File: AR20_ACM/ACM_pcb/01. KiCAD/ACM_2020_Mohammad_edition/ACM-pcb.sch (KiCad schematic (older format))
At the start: 32 parts, among them J1 TC2030-MCP-NL, P1 Conn_02x15_Odd_Even, Q1 Q_PMOS_DGS, U1 ATmega328P-AU, U2 MCP25625-x-SS, U3 NCV890430MW50TXG, Y1 16.0Mhz

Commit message: ACM-pcb full connected
ACM -12.01
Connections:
- net labels added: U-Pin29
- wire segments 103 -> 102
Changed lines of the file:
@@
 	5275 4150 5275 4225
-$Comp
-L ACM_Y2020V0.1-rescue:+12V-power #PWR015
-U 1 1 5D3DBA57
-P 6100 1175
-F 0 "#PWR015" H 6100 1025 50  0001 C CNN
-F 1 "+12V" V 6100 1375 50  0000 C CNN
-F 2 "" H 6100 1175 50  0001 C CNN
-F 3 "" H 6100 1175 50  0001 C CNN
-	1    6100 1175
-	0    -1   -1   0
-$EndComp
-$Comp
-L ACM_Y2020V0.1-rescue:+5V-power #PWR011
-U 1 1 5D3DED37
-P 5925 1475
-F 0 "#PWR011" H 5925 1325 50  0001 C CNN
-F 1 "+5V" V 5925 1650 50  0000 C CNN
-F 2 "" H 5925 1475 50  0001 C CNN
-F 3 "" H 5925 1475 50  0001 C CNN
-	1    5925 1475
-	0    -1   -1   0
-$EndComp
 $Comp
 L ACM_Y2020V0.1-rescue:GND-power #PWR016
@@
 Text HLabel 6100 1375 0    50   Input ~ 0
 U-Pin5
-Text HLabel 6100 2375 0    50   Input ~ 0
+Text HLabel 5500 2450 0    50   Input ~ 0
 U-Pin25
-Text HLabel 5675 1050 0    50   Input ~ 0
+Text HLabel 4800 1250 0    50   Input ~ 0
 U-Pin1
 Text HLabel 6100 1275 0    50   Input ~ 0
 U-Pin3
-Text HLabel 1575 6275 0    50   Input ~ 0
-U-Pin24
 Text HLabel 1400 6400 0    50   Input ~ 0
 U-Pin30
@@
 U-Pin2
 Text HLabel 2775 5475 2    50   Input ~ 0
-U-Pin7
+U-Pin1
 Text HLabel 10775 3900 2    50   Input ~ 0
 U-Pin27
 Text HLabel 10775 4200 2    50   Input ~ 0
-U-Pin1
+U-Pin29
 Wire Wire Line
 	2775 5175 3500 5175
@@
 Wire Wire Line
 	3275 6075 3450 6075
-Text HLabel 5175 2175 0    50   Input ~ 0
+Text HLabel 6100 2375 0    50   Input ~ 0
 GREEN_LED
 Text HLabel 6100 2275 0    50   Input ~ 0
@@
 Text HLabel 6600 2375 2    50   Input ~ 0
 U-Pin26
-Text HLabel 6600 2475 2    50   Input ~ 0
+Text HLabel 7000 2475 2    50   Input ~ 0
 U-Pin28
 Text HLabel 6600 1475 2    50   Input ~ 0
 U-Pin8
-Text HLabel 6100 2575 0    50   Input ~ 0
+Text HLabel 4975 2350 0    50   Input ~ 0
 Reset
 Wire Wire Line
@@
 Text HLabel 6600 1375 2    50   Input ~ 0
 U-Pin6
-Text HLabel 6600 2275 2    50   Input ~ 0
+Text HLabel 6900 2275 2    50   Input ~ 0
 U-Pin24
 Text HLabel 6600 2175 2    50   Input ~ 0
@@
 Text HLabel 5175 2050 0    50   Input ~ 0
 CLK_MCP
-Text HLabel 5300 1925 0    50   Input ~ 0
+Text HLabel 5250 1900 0    50   Input ~ 0
 RED_LED
-Text HLabel 5325 1800 0    50   Input ~ 0
+Text HLabel 6100 1975 0    50   Input ~ 0
 BLUE_LED
 Text HLabel 6100 1875 0    50   Input ~ 0
@@
 SCK
 Connection ~ 6725 1875
-Wire Wire Line
-	6100 1475 5925 1475
-Text HLabel 6600 1575 2    50   Input ~ 0
+Text HLabel 4775 1400 2    50   Input ~ 0
 U-Pin10
 Text HLabel 1575 4775 0    50   Input ~ 0
-U-Pin5
+U-Pin7
 Text HLabel 6100 2475 0    50   Input ~ 0
 U-Pin27
-Text HLabel 6100 2175 0    50   Input ~ 0
+Text HLabel 5825 2175 0    50   Input ~ 0
 U-Pin21
 Text Notes 9275 2925 0    79   ~ 16
@@
 Wire Wire Line
 	9675 2900 9675 3650
-Text HLabel 2900 5375 2    50   Input ~ 0
-U-Pin7
-Text HLabel 6600 2575 2    50   Input ~ 0
+Text HLabel 2775 5575 2    50   Input ~ 0
+U-Pin3
+Text HLabel 4650 1600 2    50   Input ~ 0
 U-Pin30
 Wire Wire Line
@@
 Wire Wire Line
 	925  4575 925  4650
-Text HLabel 6100 2075 0    50   Input ~ 0
+Text HLabel 5825 2075 0    50   Input ~ 0
 U-Pin19
-Text HLabel 6100 1975 0    50   Input ~ 0
+Text HLabel 5450 2625 0    50   Input ~ 0
 U-Pin17
-Text HLabel 6100 1575 0    50   Input ~ 0
+Text HLabel 5775 1600 0    50   Input ~ 0
 U-Pin9
 Wire Wire Line
 	2775 6075 3275 6075
 Connection ~ 3275 6075
+Text HLabel 1400 5125 0    50   Input ~ 0
+U-Pin24
+Text HLabel 6600 1575 2    50   Input ~ 0
+Reset
+Text HLabel 6100 2575 0    50   Input ~ 0
+U-Pin29
+Text HLabel 1575 4875 0    50   Input ~ 0
+U-Pin5
+$Comp
+L ACM_Y2020V0.1-rescue:+12V-power #PWR0106
+U 1 1 5E1D7493
+P 6600 2575
+F 0 "#PWR0106" H 6600 2425 50  0001 C CNN
+F 1 "+12V" V 6600 2775 50  0000 C CNN
+F 2 "" H 6600 2575 50  0001 C CNN
+F 3 "" H 6600 2575 50  0001 C CNN
+	1    6600 2575
+	0    1    1    0
+$EndComp
+$Comp
+L ACM_Y2020V0.1-rescue:+12V-power #PWR015
+U 1 1 5D3DBA57
+P 5050 1150
+F 0 "#PWR015" H 5050 1000 50  0001 C CNN
+F 1 "+12V" V 5050 1750 50  0000 C CNN
+F 2 "" H 5050 1150 50  0001 C CNN
+F 3 "" H 5050 1150 50  0001 C CNN
+	1    5050 1150
+	0    -1   -1   0
+$EndComp
+Text HLabel 6100 1175 0    50   Input ~ 0
+U-Pin1
+$Comp
+L ACM_Y2020V0.1-rescue:+5V-power #PWR011
+U 1 1 5D3DED37
+P 6600 2475
+F 0 "#PWR011" H 6600 2325 50  0001 C CNN
+F 1 "+5V" V 6600 2650 50  0000 C CNN
+F 2 "" H 6600 2475 50  0001 C CNN
+F 3 "" H 6600 2475 50  0001 C CNN
+	1    6600 2475
+	0    1    1    0
+$EndComp
+Text HLabel 6100 1475 0    50   Input ~ 0
+U-Pin7
+$Comp
+L ACM_Y2020V0.1-rescue:GND-power #PWR0107
+U 1 1 5E243E92
+P 6600 2275
+F 0 "#PWR0107" H 6600 2025 50  0001 C CNN
+F 1 "GND" H 6605 2102 50  0000 C CNN
+F 2 "" H 6600 2275 50  0001 C CNN
+F 3 "" H 6600 2275 50  0001 C CNN
+	1    6600 2275
+	0    -1   -1   0
+$EndComp
+$Comp
+L ACM_Y2020V0.1-rescue:GND-power #PWR?
+U 1 1 5E24CDDB
+P 6100 2175
+F 0 "#PWR?" H 6100 1925 50  0001 C CNN
+F 1 "GND" H 6105 2002 50  0000 C CNN
+F 2 "" H 6100 2175 50  0001 C CNN
+F 3 "" H 6100 2175 50  0001 C CNN
+	1    6100 2175
+	0    1    1    0
+$EndComp
 $EndSCHEMATC

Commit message: final one 12.01
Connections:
- wire segments 102 -> 110
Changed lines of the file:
@@
 Wire Wire Line
 	6600 1875 6725 1875
-Text HLabel 6600 2375 2    50   Input ~ 0
+Text HLabel 8000 2400 2    50   Input ~ 0
 U-Pin26
-Text HLabel 7000 2475 2    50   Input ~ 0
+Text HLabel 7375 2525 2    50   Input ~ 0
 U-Pin28
 Text HLabel 6600 1475 2    50   Input ~ 0
@@
 Text HLabel 6600 1375 2    50   Input ~ 0
 U-Pin6
-Text HLabel 6900 2275 2    50   Input ~ 0
+Text HLabel 7875 2250 2    50   Input ~ 0
 U-Pin24
 Text HLabel 6600 2175 2    50   Input ~ 0
@@
 Text HLabel 6100 2475 0    50   Input ~ 0
 U-Pin27
-Text HLabel 5825 2175 0    50   Input ~ 0
+Text HLabel 5325 2175 0    50   Input ~ 0
 U-Pin21
 Text Notes 9275 2925 0    79   ~ 16
@@
 Text HLabel 5450 2625 0    50   Input ~ 0
 U-Pin17
-Text HLabel 5775 1600 0    50   Input ~ 0
+Text HLabel 6100 1575 0    50   Input ~ 0
 U-Pin9
 Wire Wire Line
@@
 L ACM_Y2020V0.1-rescue:+12V-power #PWR0106
 U 1 1 5E1D7493
-P 6600 2575
-F 0 "#PWR0106" H 6600 2425 50  0001 C CNN
-F 1 "+12V" V 6600 2775 50  0000 C CNN
-F 2 "" H 6600 2575 50  0001 C CNN
-F 3 "" H 6600 2575 50  0001 C CNN
-	1    6600 2575
+P 6800 2575
+F 0 "#PWR0106" H 6800 2425 50  0001 C CNN
+F 1 "+12V" V 6800 2775 50  0000 C CNN
+F 2 "" H 6800 2575 50  0001 C CNN
+F 3 "" H 6800 2575 50  0001 C CNN
+	1    6800 2575
 	0    1    1    0
 $EndComp
@@
 Text HLabel 6100 1175 0    50   Input ~ 0
 U-Pin1
-$Comp
-L ACM_Y2020V0.1-rescue:+5V-power #PWR011
-U 1 1 5D3DED37
-P 6600 2475
-F 0 "#PWR011" H 6600 2325 50  0001 C CNN
-F 1 "+5V" V 6600 2650 50  0000 C CNN
-F 2 "" H 6600 2475 50  0001 C CNN
-F 3 "" H 6600 2475 50  0001 C CNN
-	1    6600 2475
-	0    1    1    0
-$EndComp
 Text HLabel 6100 1475 0    50   Input ~ 0
 U-Pin7
@@
 L ACM_Y2020V0.1-rescue:GND-power #PWR0107
 U 1 1 5E243E92
-P 6600 2275
-F 0 "#PWR0107" H 6600 2025 50  0001 C CNN
-F 1 "GND" H 6605 2102 50  0000 C CNN
-F 2 "" H 6600 2275 50  0001 C CNN
-F 3 "" H 6600 2275 50  0001 C CNN
-	1    6600 2275
+P 7325 2125
+F 0 "#PWR0107" H 7325 1875 50  0001 C CNN
+F 1 "GND" H 7330 1952 50  0000 C CNN
+F 2 "" H 7325 2125 50  0001 C CNN
+F 3 "" H 7325 2125 50  0001 C CNN
+	1    7325 2125
 	0    -1   -1   0
 $EndComp
 $Comp
-L ACM_Y2020V0.1-rescue:GND-power #PWR?
+L ACM_Y2020V0.1-rescue:GND-power #PWR0108
 U 1 1 5E24CDDB
-P 6100 2175
-F 0 "#PWR?" H 6100 1925 50  0001 C CNN
-F 1 "GND" H 6105 2002 50  0000 C CNN
-F 2 "" H 6100 2175 50  0001 C CNN
-F 3 "" H 6100 2175 50  0001 C CNN
-	1    6100 2175
+P 6050 2175
+F 0 "#PWR0108" H 6050 1925 50  0001 C CNN
+F 1 "GND" H 6055 2002 50  0000 C CNN
+F 2 "" H 6050 2175 50  0001 C CNN
+F 3 "" H 6050 2175 50  0001 C CNN
+	1    6050 2175
 	0    1    1    0
 $EndComp
+$Comp
+L ACM_Y2020V0.1-rescue:+5V-power #PWR011
+U 1 1 5D3DED37
+P 6700 2375
+F 0 "#PWR011" H 6700 2225 50  0001 C CNN
+F 1 "+5V" V 6700 2550 50  0000 C CNN
+F 2 "" H 6700 2375 50  0001 C CNN
+F 3 "" H 6700 2375 50  0001 C CNN
+	1    6700 2375
+	0    1    1    0
+$EndComp
+Wire Wire Line
+	6700 2375 6600 2375
+Wire Wire Line
+	6600 2275 6700 2275
+Wire Wire Line
+	6700 2275 6700 2375
+Connection ~ 6700 2375
+Wire Wire Line
+	6600 2575 6800 2575
+Wire Wire Line
+	6600 2475 6700 2475
+Wire Wire Line
+	6700 2475 6700 2375
+Wire Wire Line
+	6100 2075 6100 2175
+Wire Wire Line
+	6100 2175 6050 2175
+Connection ~ 6100 2175
 $EndSCHEMATC

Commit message: Ronded corner and added a angle
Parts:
- C1, C10, C11, C2, C4, C5, C6, C7, C8, C9: symbol ACM_Y2020V0.1-rescue:C-Device -> ACM-pcb-rescue:C-Device-ACM_Y2020V0.1-rescue
- C3: symbol ACM_Y2020V0.1-rescue:C_Small-Device -> ACM-pcb-rescue:C_Small-Device-ACM_Y2020V0.1-rescue
- D1, D2: symbol ACM_Y2020V0.1-rescue:D_Zener-Device -> ACM-pcb-rescue:D_Zener-Device-ACM_Y2020V0.1-rescue
- D3: symbol ACM_Y2020V0.1-rescue:ASMB-MTB0-0A3A2-LED -> ACM-pcb-rescue:ASMB-MTB0-0A3A2-LED-ACM_Y2020V0.1-rescue
- F1: symbol ACM_Y2020V0.1-rescue:Polyfuse_Small-Device -> ACM-pcb-rescue:Polyfuse_Small-Device-ACM_Y2020V0.1-rescue
- H1: symbol ACM_Y2020V0.1-rescue:MountingHole-Mechanical -> ACM-pcb-rescue:MountingHole-Mechanical-ACM_Y2020V0.1-rescue
- J1: symbol ACM_Y2020V0.1-rescue:TC2030-MCP-NL-TC2030-MCP-NL -> ACM-pcb-rescue:TC2030-MCP-NL-TC2030-MCP-NL-ACM_Y2020V0.1-rescue
- L1, L2: symbol ACM_Y2020V0.1-rescue:L_Small-Device -> ACM-pcb-rescue:L_Small-Device-ACM_Y2020V0.1-rescue
- P1: symbol ACM_Y2020V0.1-rescue:Conn_02x15_Odd_Even-Connector_Generic -> ACM-pcb-rescue:Conn_02x15_Odd_Even-Connector_Generic-ACM_Y2020V0.1-rescue
- Q1: symbol ACM_Y2020V0.1-rescue:Q_PMOS_GSD-Device -> ACM-pcb-rescue:Q_PMOS_GSD-Device-ACM_Y2020V0.1-rescue
- R1, R2, R3, R4, R5, R6, R7: symbol ACM_Y2020V0.1-rescue:R-Device -> ACM-pcb-rescue:R-Device-ACM_Y2020V0.1-rescue
- U1: symbol ACM_Y2020V0.1-rescue:ATmega328P-AU-MCU_Microchip_ATmega -> ACM-pcb-rescue:ATmega328P-AU-MCU_Microchip_ATmega-ACM_Y2020V0.1-rescue
- U2: symbol ACM_Y2020V0.1-rescue:MCP25625-x-SS-Interface_CAN_LIN -> ACM-pcb-rescue:MCP25625-x-SS-Interface_CAN_LIN-ACM_Y2020V0.1-rescue
- U3: symbol ACM_Y2020V0.1-rescue:NCV890430MW50TXG-NCV890430MW50TXG -> ACM-pcb-rescue:NCV890430MW50TXG-NCV890430MW50TXG-ACM_Y2020V0.1-rescue
- Y1: symbol ACM_Y2020V0.1-rescue:Resonator_Small-Device -> ACM-pcb-rescue:Resonator_Small-Device-ACM_Y2020V0.1-rescue

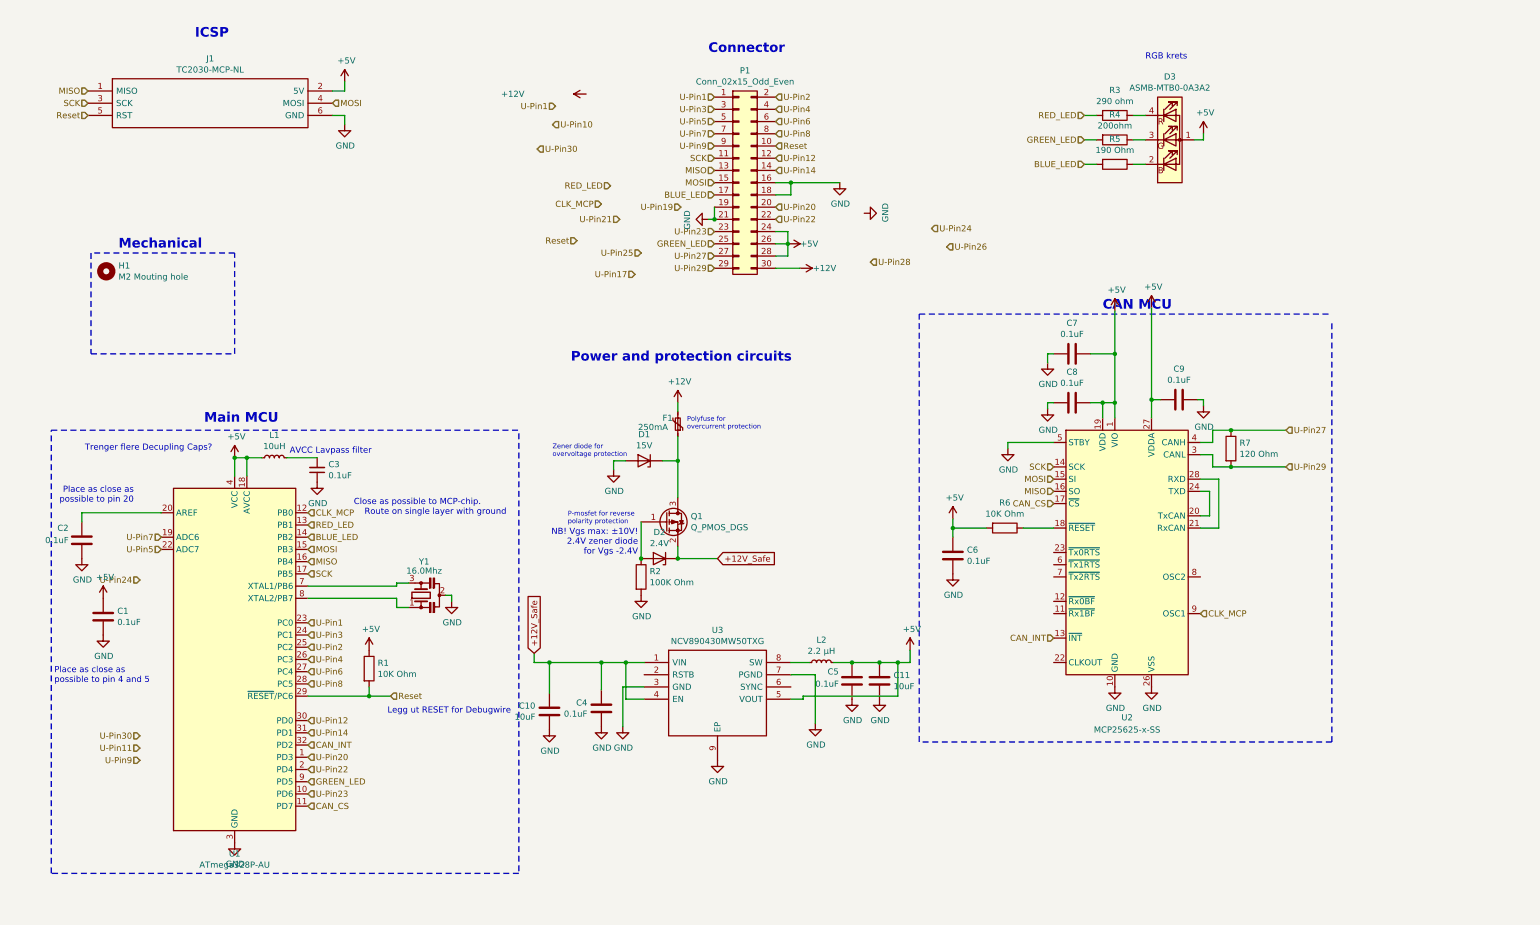
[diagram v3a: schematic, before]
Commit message: Added GND to Pin 9 and checked connector output
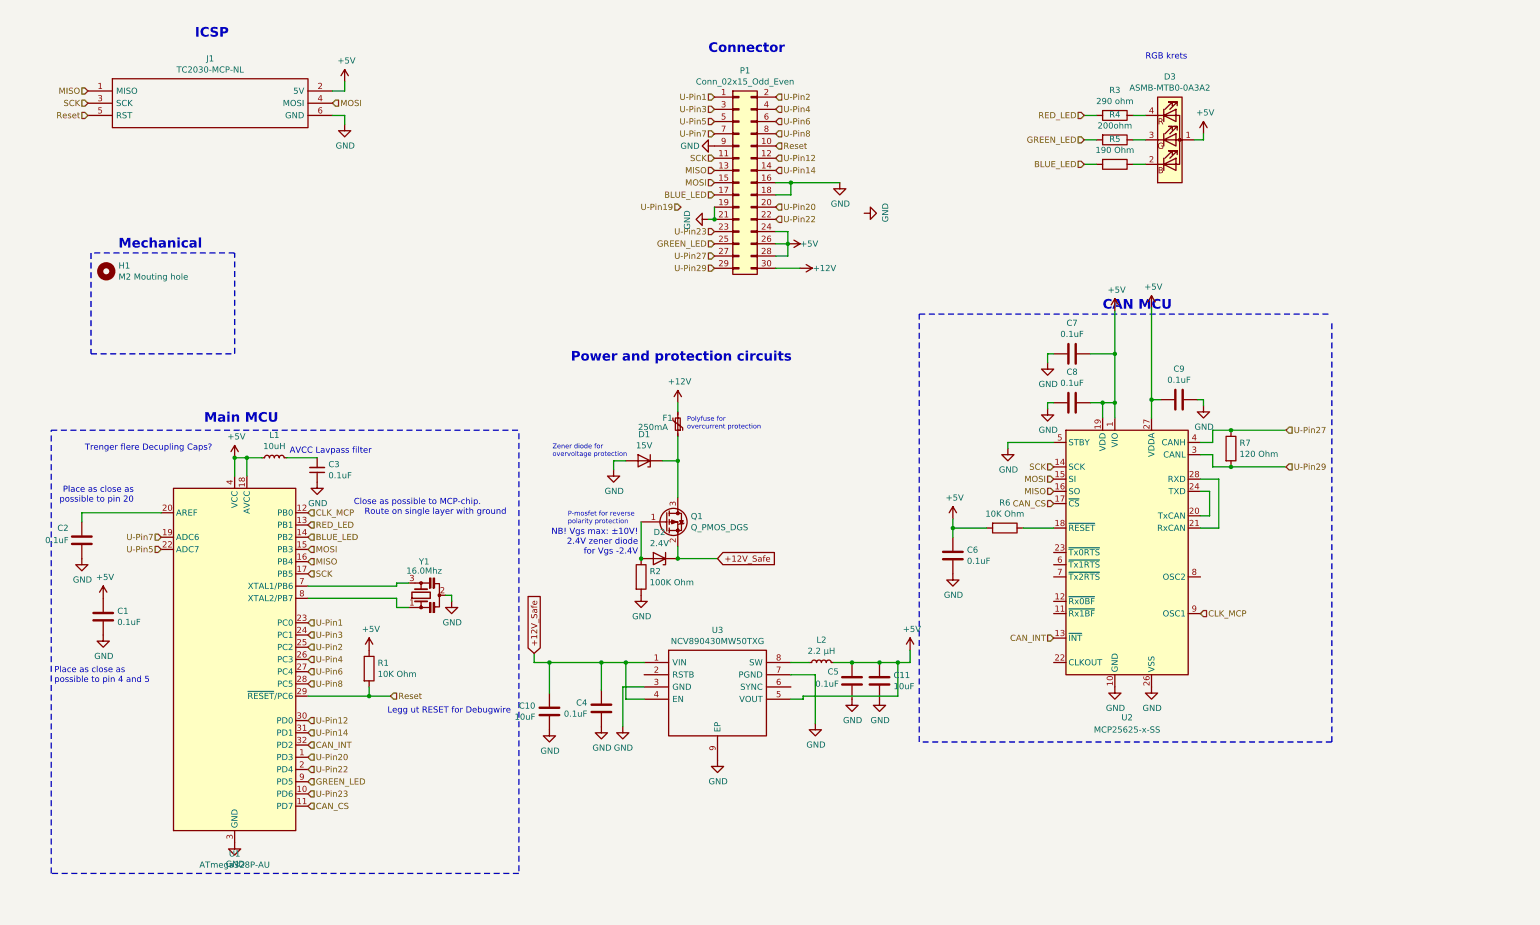
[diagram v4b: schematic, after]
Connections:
- net U-Pin9 is gone; now on net GND: P1.9 (Pin_9)
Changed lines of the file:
@@
 Text HLabel 6100 1375 0    50   Input ~ 0
 U-Pin5
-Text HLabel 5500 2450 0    50   Input ~ 0
-U-Pin25
-Text HLabel 4800 1250 0    50   Input ~ 0
-U-Pin1
 Text HLabel 6100 1275 0    50   Input ~ 0
 U-Pin3
-Text HLabel 1400 6400 0    50   Input ~ 0
-U-Pin30
-Text HLabel 1400 6500 0    50   Input ~ 0
-U-Pin11
-Text HLabel 1400 6600 0    50   Input ~ 0
-U-Pin9
 Text HLabel 2775 6675 2    50   Input ~ 0
 U-Pin22
@@
 Wire Wire Line
 	6600 1875 6725 1875
-Text HLabel 8000 2400 2    50   Input ~ 0
-U-Pin26
-Text HLabel 7375 2525 2    50   Input ~ 0
-U-Pin28
 Text HLabel 6600 1475 2    50   Input ~ 0
 U-Pin8
-Text HLabel 4975 2350 0    50   Input ~ 0
-Reset
 Wire Wire Line
 	6725 1875 7125 1875
 Text HLabel 6600 1375 2    50   Input ~ 0
 U-Pin6
-Text HLabel 7875 2250 2    50   Input ~ 0
-U-Pin24
 Text HLabel 6600 2175 2    50   Input ~ 0
 U-Pin22
@@
 	1    0    0    -1
 $EndComp
-Text HLabel 5175 2050 0    50   Input ~ 0
-CLK_MCP
-Text HLabel 5250 1900 0    50   Input ~ 0
-RED_LED
 Text HLabel 6100 1975 0    50   Input ~ 0
 BLUE_LED
@@
 SCK
 Connection ~ 6725 1875
-Text HLabel 4775 1400 2    50   Input ~ 0
-U-Pin10
 Text HLabel 1575 4775 0    50   Input ~ 0
 U-Pin7
 Text HLabel 6100 2475 0    50   Input ~ 0
 U-Pin27
-Text HLabel 5325 2175 0    50   Input ~ 0
-U-Pin21
 Text Notes 9275 2925 0    79   ~ 16
 CAN MCU
@@
 Text HLabel 2775 5575 2    50   Input ~ 0
 U-Pin3
-Text HLabel 4650 1600 2    50   Input ~ 0
-U-Pin30
 Wire Wire Line
 	1575 4575 925  4575
@@
 Text HLabel 5825 2075 0    50   Input ~ 0
 U-Pin19
-Text HLabel 5450 2625 0    50   Input ~ 0
-U-Pin17
-Text HLabel 6100 1575 0    50   Input ~ 0
-U-Pin9
 Wire Wire Line
 	2775 6075 3275 6075
 Connection ~ 3275 6075
-Text HLabel 1400 5125 0    50   Input ~ 0
-U-Pin24
 Text HLabel 6600 1575 2    50   Input ~ 0
 Reset
@@
 	0    1    1    0
 $EndComp
-$Comp
-L ACM-pcb-rescue:+12V-power-ACM_Y2020V0.1-rescue #PWR015
-U 1 1 5D3DBA57
-P 5050 1150
-F 0 "#PWR015" H 5050 1000 50  0001 C CNN
-F 1 "+12V" V 5050 1750 50  0000 C CNN
-F 2 "" H 5050 1150 50  0001 C CNN
-F 3 "" H 5050 1150 50  0001 C CNN
-	1    5050 1150
-	0    -1   -1   0
-$EndComp
 Text HLabel 6100 1175 0    50   Input ~ 0
 U-Pin1
@@
 	6100 2175 6050 2175
 Connection ~ 6100 2175
+$Comp
+L ACM-pcb-rescue:GND-power-ACM_Y2020V0.1-rescue #PWR?
+U 1 1 5E1CB20B
+P 6100 1575
+F 0 "#PWR?" H 6100 1325 50  0001 C CNN
+F 1 "GND" V 6100 1375 50  0000 C CNN
+F 2 "" H 6100 1575 50  0001 C CNN
+F 3 "" H 6100 1575 50  0001 C CNN
+	1    6100 1575
+	0    1    1    0
+$EndComp
 $EndSCHEMATC

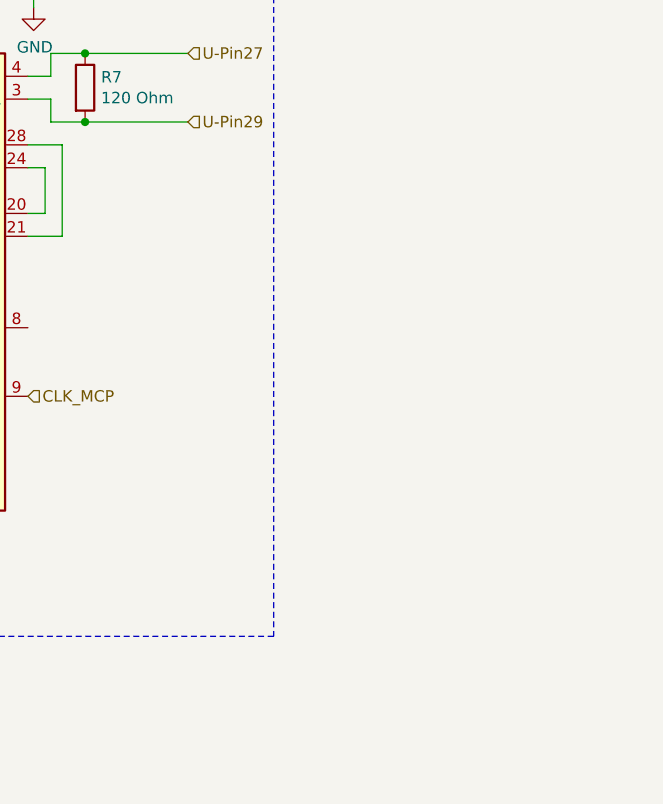
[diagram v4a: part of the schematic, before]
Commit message: Added correct MCP25625 symbol - Need to be converted in schematic
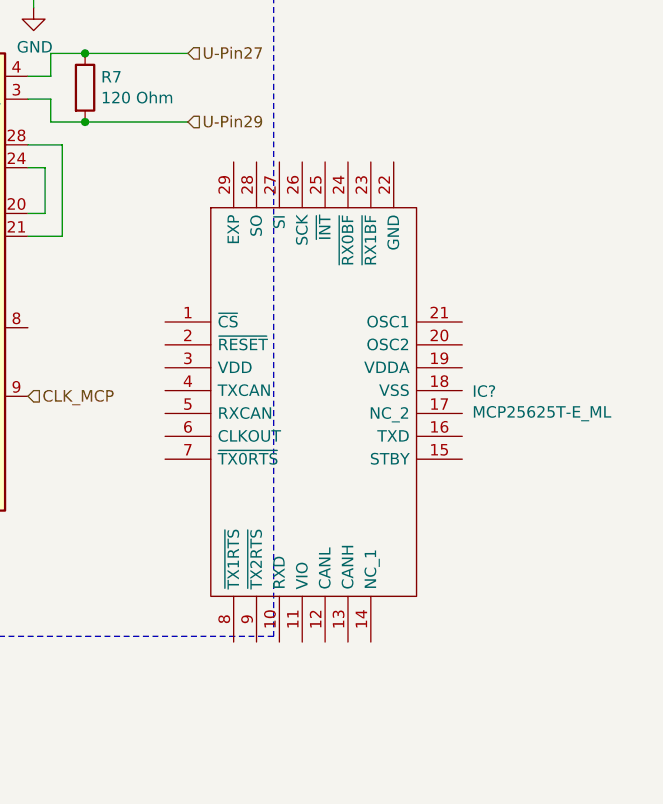
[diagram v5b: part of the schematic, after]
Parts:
- added IC?: MCP25625T-E_ML, QFN65P600X600X100-29N-D, symbol ACM-pcb-rescue:MCP25625T-E_ML
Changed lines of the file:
@@
 	0    1    1    0
 $EndComp
+$Comp
+L ACM-pcb-rescue:MCP25625T-E_ML IC?
+U 1 1 5E5FCA78
+P 10675 5075
+F 0 "IC?" H 12019 4771 50  0000 L CNN
+F 1 "MCP25625T-E_ML" H 12019 4680 50  0000 L CNN
+F 2 "QFN65P600X600X100-29N-D" H 11825 5575 50  0001 L CNN
+F 3 "https://www.mouser.com/datasheet/2/268/20005282B-708896.pdf" H 11825 5475 50  0001 L CNN
+F 4 "Microchip Technology MCP25625T-E/ML, CAN Controller 1Mbit/s CAN 2.0B, 28-Pin QFN" H 11825 5375 50  0001 L CNN "Description"
+F 5 "1" H 11825 5275 50  0001 L CNN "Height"
+F 6 "Microchip" H 11825 5175 50  0001 L CNN "Manufacturer_Name"
+F 7 "MCP25625T-E/ML" H 11825 5075 50  0001 L CNN "Manufacturer_Part_Number"
+F 8 "579-MCP25625T-E/ML" H 11825 4975 50  0001 L CNN "Mouser Part Number"
+F 9 "https://www.mouser.com/Search/Refine.aspx?Keyword=579-MCP25625T-E%2FML" H 11825 4875 50  0001 L CNN "Mouser Price/Stock"
+F 10 "1773171P" H 11825 4775 50  0001 L CNN "RS Part Number"
+F 11 "http://uk.rs-online.com/web/p/products/1773171P" H 11825 4675 50  0001 L CNN "RS Price/Stock"
+F 12 "70568355" H 11825 4575 50  0001 L CNN "Allied_Number"
+F 13 "https://www.alliedelec.com/microchiptechnologyinc-mcp25625t-e-ml/70568355/" H 11825 4475 50  0001 L CNN "Allied Price/Stock"
+	1    10675 5075
+	1    0    0    -1
+$EndComp
 $EndSCHEMATC
